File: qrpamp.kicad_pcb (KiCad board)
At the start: 2 copper layers, 152.4 x 88.9 mm, 113 parts, among them K1 BAND3_IN, K2 BAND2_IN, K3 BAND1_IN, K4 BAND3_OUT, K5 BAND2_OUT, K6 BAND1_OUT, K7 ANT_RLY, P1 PWR, P2 PWR_SW, P3 SWD, P4 ANT, P5 RADIO, P6 PTT_IN, P7 TP, P8 NAV_BUTTON, Q1 MMBT6427, Q10 MMBF170, Q11 MMBF170, Q2 MMBF170, Q3 IRF510, Q4 IRF510, Q6 MMBF170, Q9 MMBF170, SW1 SW_PUSH, T1 8:8, T2 8:8, T3 2:3, T4 12:1, T5 1:12, U1 LM7805, U2 LM3940, U3 LCD-2x16, U4 STM32F401xB/C-LQFP

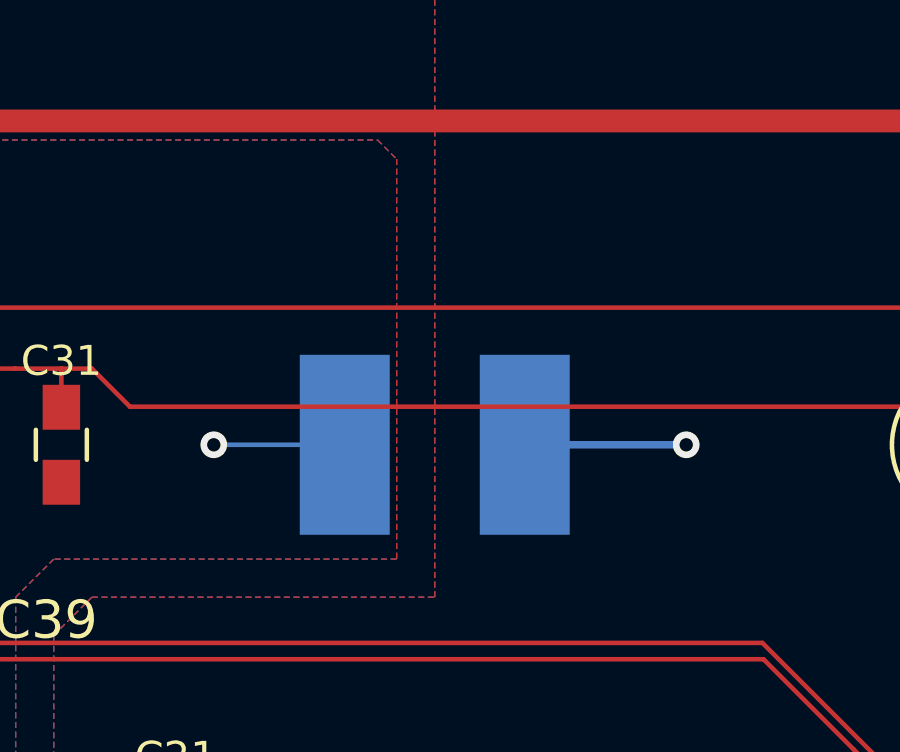
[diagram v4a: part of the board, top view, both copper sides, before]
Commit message: Closes #4: extend chassis pads
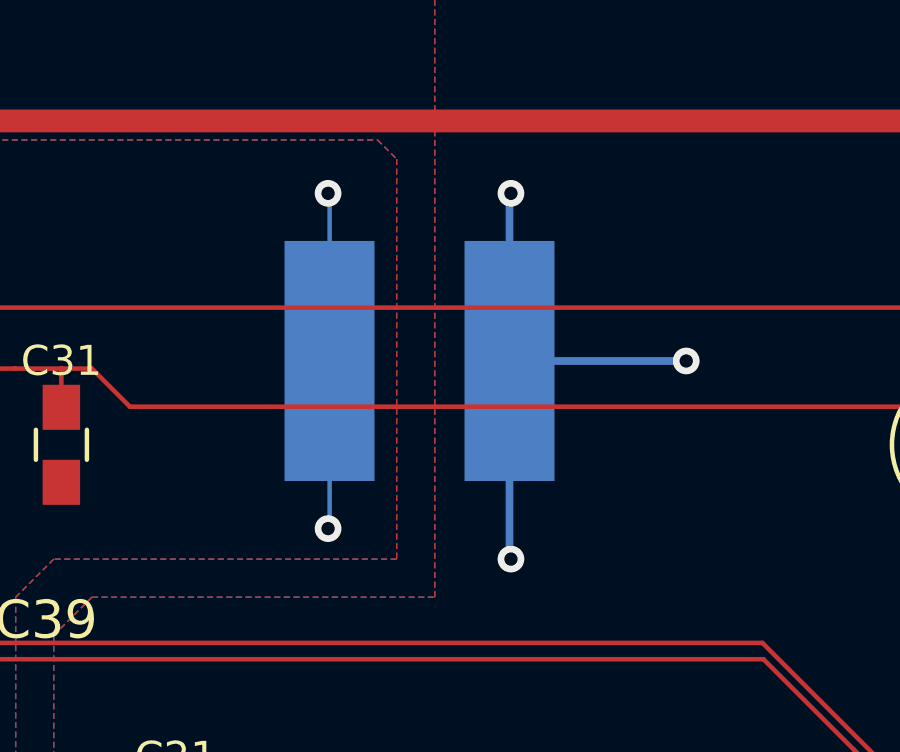
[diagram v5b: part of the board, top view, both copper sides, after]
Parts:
- moved L9 2.84 mm to (132.8, 55.6)
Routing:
- net GND: track 61.4 -> 74.1 mm, vias 13 -> 15
- net DGND: track 27.2 -> 34.0 mm, vias 7 -> 8
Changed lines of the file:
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@@
     (thickness 1.6)
     (drawings 26)
-    (tracks 693)
+    (tracks 703)
     (zones 0)
     (modules 113)
@@
     (mod_text_size 1.5 1.5)
     (mod_text_width 0.15)
-    (pad_size 0.8001 1.80086)
+    (pad_size 2.99974 8)
     (pad_drill 0)
     (pad_to_mask_clearance 0.2)
@@
   )
   (module nu9j-footprints:WE-SUCKW (layer B.Cu)
-    (at 133.35 58.42 180)
+    (at 132.842 55.626 180)
     (fp_text reference L9 (at 0 5.00126 180) (layer B.SilkS)
       (effects (font (thickness 0.3048)) (justify mirror))
@@
     (fp_line (start 5.99948 -2.49936) (end 5.99948 2.49936) (layer B.SilkS) (width 0.381))
     (fp_line (start 5.99948 2.49936) (end -5.99948 2.49936) (layer B.SilkS) (width 0.381))
-    (pad 1 smd rect (at -2.99974 0 180) (size 2.99974 5.99948) (layers B.Cu B.Paste B.Mask)
+    (pad 1 smd rect (at -2.99974 0 180) (size 2.99974 8) (layers B.Cu B.Paste B.Mask)
       (net 3 GND))
-    (pad 2 smd rect (at 2.99974 0 180) (size 2.99974 5.99948) (layers B.Cu B.Paste B.Mask)
+    (pad 2 smd rect (at 2.99974 0 180) (size 2.99974 8) (layers B.Cu B.Paste B.Mask)
       (net 85 DGND))
   )
@@
   (segment (start 206.756 102.87) (end 213.36 102.87) (width 0.2794) (layer F.Cu) (net 2))
   (segment (start 209.53 92.71) (end 211.582 92.71) (width 0.2794) (layer F.Cu) (net 2))
+  (segment (start 135.84174 55.626) (end 135.84174 50.08626) (width 0.254) (layer B.Cu) (net 3))
+  (via (at 135.89 50.038) (size 0.889) (layers F.Cu B.Cu) (net 3))
+  (segment (start 135.84174 50.08626) (end 135.89 50.038) (width 0.254) (layer B.Cu) (net 3))
+  (segment (start 135.84174 55.626) (end 135.84174 62.18174) (width 0.254) (layer B.Cu) (net 3))
+  (via (at 135.89 62.23) (size 0.889) (layers F.Cu B.Cu) (net 3))
+  (segment (start 135.84174 62.18174) (end 135.89 62.23) (width 0.254) (layer B.Cu) (net 3))
+  (segment (start 135.84174 55.626) (end 141.732 55.626) (width 0.254) (layer B.Cu) (net 3))
+  (via (at 141.732 55.626) (size 0.889) (layers F.Cu B.Cu) (net 3))
   (segment (start 215.41486 109.662) (end 215.41486 111.02086) (width 0.254) (layer F.Cu) (net 3))
   (via (at 216.662 112.268) (size 0.889) (layers F.Cu B.Cu) (net 3))
@@
   (via (at 185.42 124.714) (size 0.889) (layers F.Cu B.Cu) (net 3))
   (segment (start 185.42 121.38) (end 185.42 124.714) (width 0.254) (layer F.Cu) (net 3))
-  (via (at 141.732 58.42) (size 0.889) (layers F.Cu B.Cu) (net 3))
-  (segment (start 136.34974 58.42) (end 141.732 58.42) (width 0.254) (layer B.Cu) (net 3))
   (segment (start 197.58 78.74) (end 197.58 82.55) (width 0.254) (layer F.Cu) (net 4))
   (segment (start 201.95 78.74) (end 197.58 78.74) (width 0.254) (layer F.Cu) (net 4))
@@
   (segment (start 100.838 70.358) (end 103.632 70.358) (width 0.1524) (layer F.Cu) (net 79))
   (segment (start 100.484 70.004) (end 100.838 70.358) (width 0.1524) (layer F.Cu) (net 79))
+  (segment (start 129.84226 55.626) (end 129.84226 61.16574) (width 0.1524) (layer B.Cu) (net 85))
+  (via (at 129.794 61.214) (size 0.889) (layers F.Cu B.Cu) (net 85))
+  (segment (start 129.84226 61.16574) (end 129.794 61.214) (width 0.1524) (layer B.Cu) (net 85))
+  (segment (start 129.84226 55.626) (end 129.84226 50.08626) (width 0.1524) (layer B.Cu) (net 85))
+  (via (at 129.794 50.038) (size 0.889) (layers F.Cu B.Cu) (net 85))
+  (segment (start 129.84226 50.08626) (end 129.794 50.038) (width 0.1524) (layer B.Cu) (net 85))
   (segment (start 109.22 58.4) (end 109.22 60.198) (width 0.1524) (layer F.Cu) (net 85))
   (via (at 109.982 60.96) (size 0.889) (layers F.Cu B.Cu) (net 85))
@@
   (via (at 92.075 55.88) (size 0.889) (layers F.Cu B.Cu) (net 85))
   (segment (start 92.476 53.594) (end 92.476 55.479) (width 0.1524) (layer F.Cu) (net 85))
-  (via (at 125.984 58.42) (size 0.889) (layers F.Cu B.Cu) (net 85))
-  (segment (start 130.35026 58.42) (end 125.984 58.42) (width 0.1524) (layer B.Cu) (net 85))
   (segment (start 130.81 116.84) (end 130.81 111.76) (width 0.254) (layer F.Cu) (net 86))
   (segment (start 128.27 109.22) (end 128.27 101.6) (width 0.254) (layer F.Cu) (net 86))

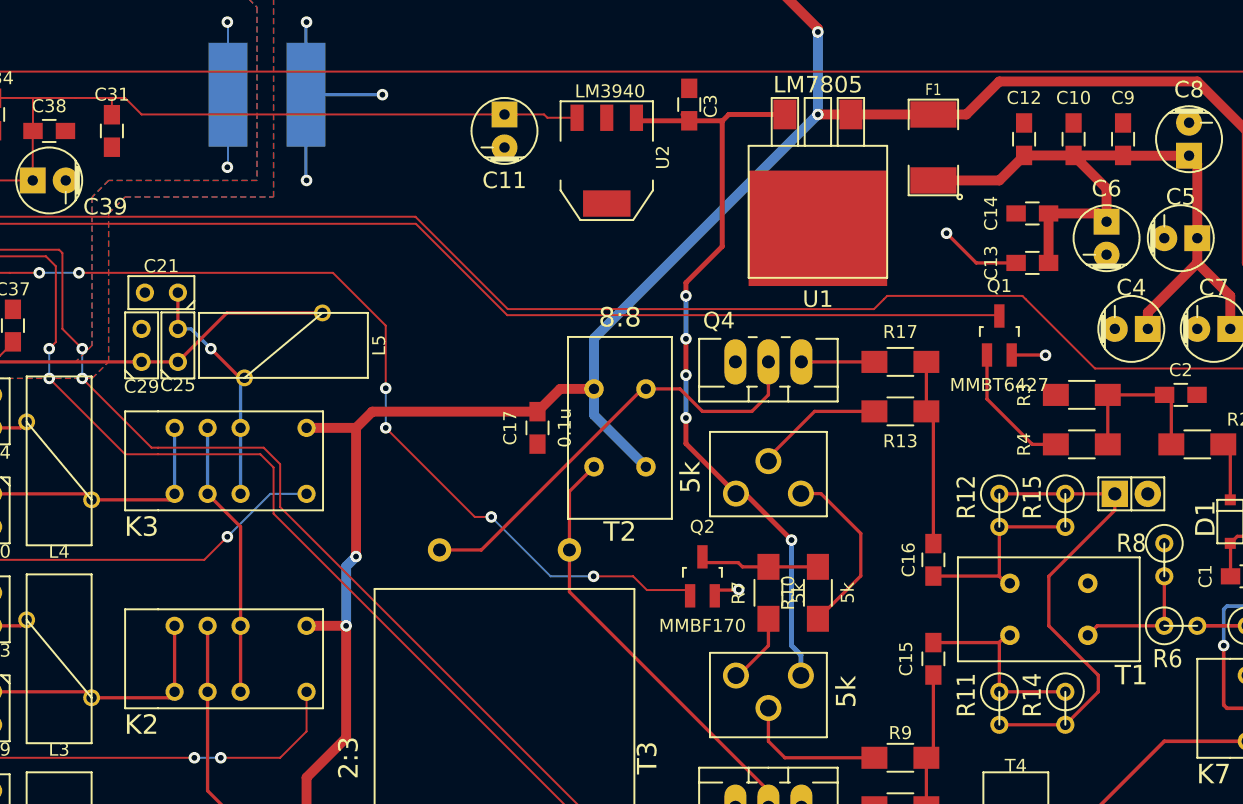
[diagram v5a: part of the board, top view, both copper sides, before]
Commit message: Fixes #9: gate bias broken
Replaces Q2 with LTV-356T opto-coupler between 5V and bias rail
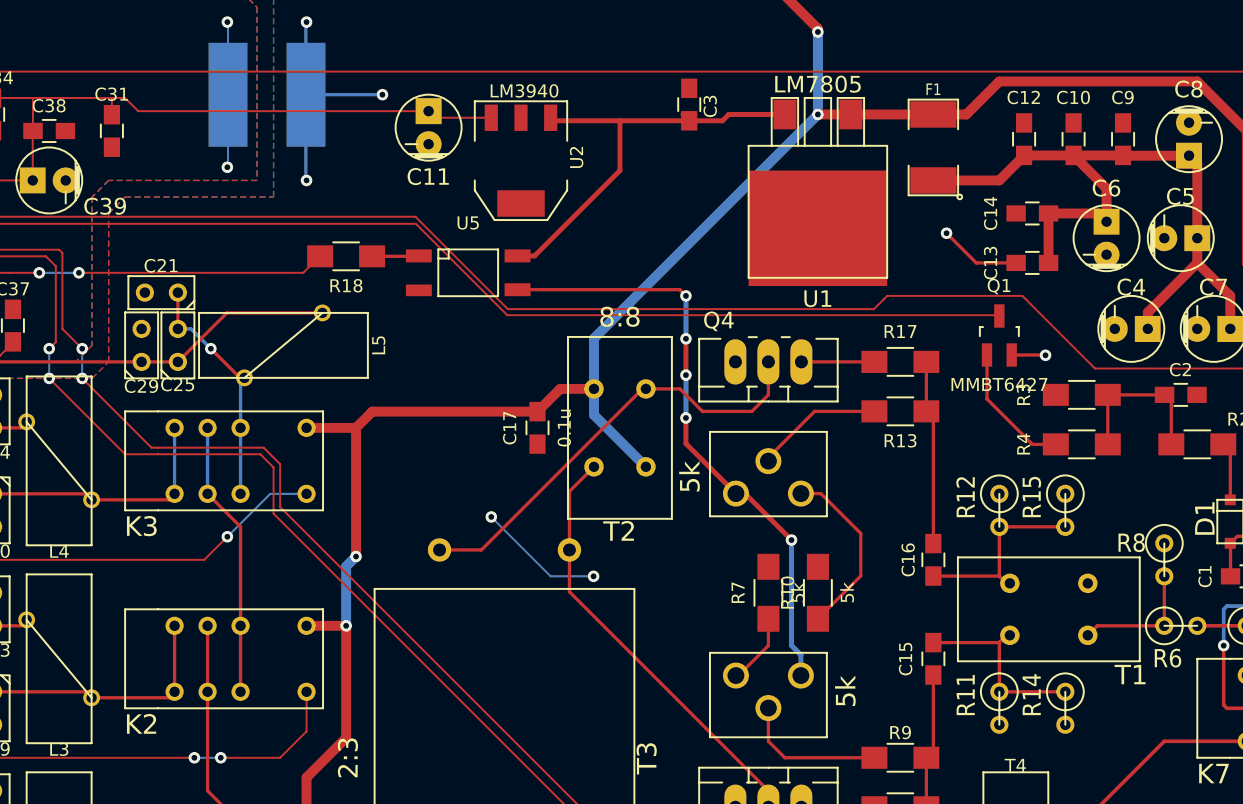
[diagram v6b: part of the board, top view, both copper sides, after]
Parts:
- removed JP1: AMP_BAL, Pin_Headers:Pin_Header_Straight_1x02
- removed Q2: MMBF170, nu9j-footprints:SOT-23-DGS_HandSoldering
- added R18: 150, Resistors_SMD:R_1206_HandSoldering, F.Cu at (138.9, 68.1)
- added U5: LTV-356T, Opto-Devices:Optocoupler_SMD_HandSoldering_KPC357_LTV35x_PC357_SingleChannel, F.Cu at (148.3, 69.3)
- moved U2 6.60 mm to (152.4, 60.7)
- moved C11 5.85 mm to (145.3, 58.2)
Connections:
- R10 pad 2: Net-(Q2-PadD) -> GND
- R11 pad 2: Net-(JP1-Pad1) -> GND
- R12 pad 1: Net-(JP1-Pad1) -> GND
- R14 pad 2: Net-(JP1-Pad1) -> GND
- R15 pad 1: Net-(JP1-Pad1) -> GND
- R7 pad 2: Net-(Q2-PadD) -> GND
- RV1 pad 1: +5V -> Net-(RV1-Pad1)
- RV2 pad 1: +5V -> Net-(RV1-Pad1)
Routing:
- net Net-(RV1-Pad1): track 0.00 -> 46.5 mm, vias 0 -> 5
- net /Amplifier/amp_on: track 85.5 -> 42.8 mm, vias 6 -> 2
- net Net-(JP1-Pad1): track 36.5 -> 0.00 mm
- net +5V: track 60.4 -> 33.5 mm, vias 5 -> 0
- net (no net): track 0.02 -> 9.79 mm, vias 0 -> 2
- net Net-(Q2-PadD): track 9.49 -> 0.00 mm
- net +3.3V: track 146.8 -> 140.2 mm
- net Net-(R18-Pad1): track 0.00 -> 3.61 mm
- net GND: track 74.1 -> 72.7 mm, vias 15 -> 14

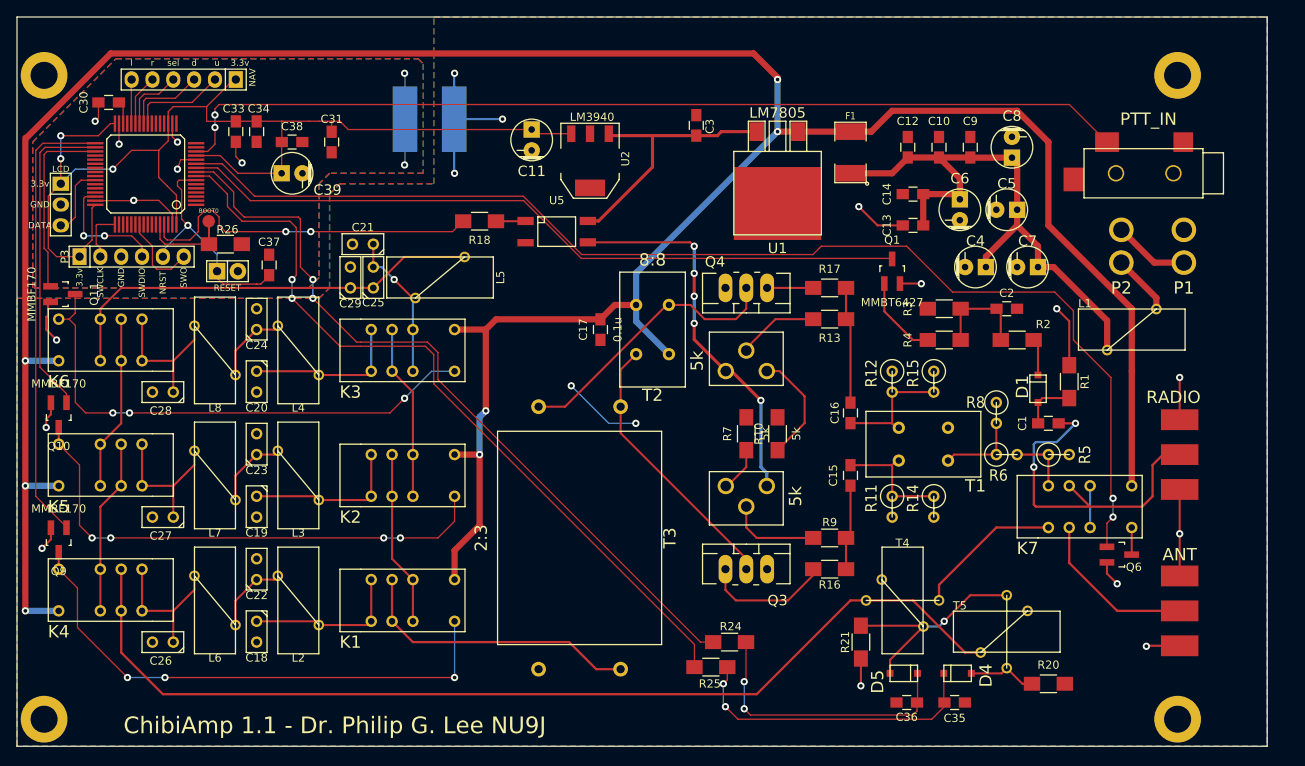
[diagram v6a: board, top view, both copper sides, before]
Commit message: Fixes #8: transistor placement
Also, this is a major board layout change

- Added more 12V filtering caps
- Placed fuse in front of filtering caps
- Changed IRF510 footprints to horizontal lower side w/ mounting hole
- Expanded layout to fill new board size
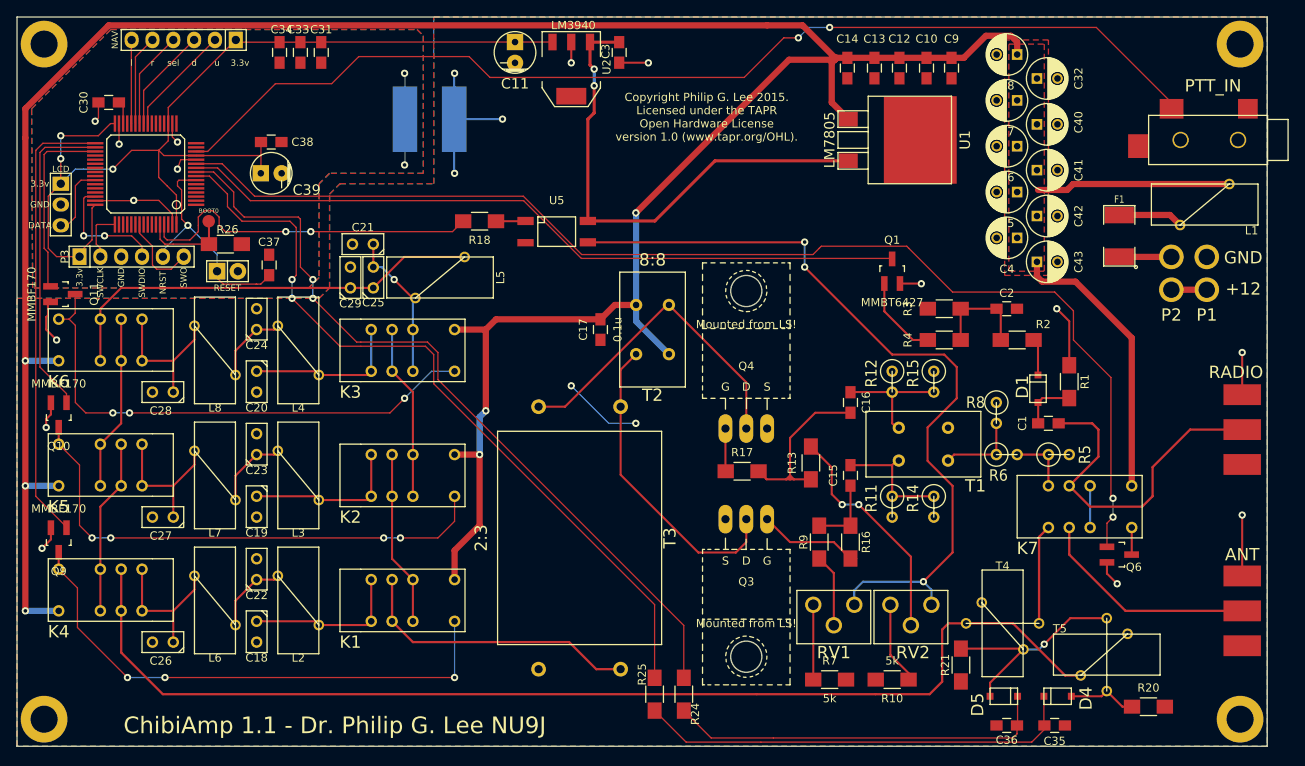
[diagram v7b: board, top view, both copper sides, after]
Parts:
- added C32: 10u, Capacitors_ThroughHole:C_Radial_D5_L11_P2.5, F.Cu at (206.9, 50.7)
- added C40: 10u, Capacitors_ThroughHole:C_Radial_D5_L11_P2.5, F.Cu at (206.9, 56.3)
- added C41: 10u, Capacitors_ThroughHole:C_Radial_D5_L11_P2.5, F.Cu at (206.9, 61.8)
- added C42: 10u, Capacitors_ThroughHole:C_Radial_D5_L11_P2.5, F.Cu at (206.9, 67.4)
- added C43: 10u, Capacitors_ThroughHole:C_Radial_D5_L11_P2.5, F.Cu at (206.9, 73.0)
- C4, C5, C6, C7, C8: footprint Capacitors_ThroughHole:Capacitor5x11RM2.5 -> Capacitors_ThroughHole:C_Radial_D5_L11_P2.5
- F1: value PTS181224V150 -> PTS18128V200
- Q3, Q4: footprint Transistors_TO-220:TO-220_FET-GDS_Vertical_LargePads -> Transistors_TO-220:TO-220_FET-GDS_Horizontal_MountedFromLS_LargePads
- moved RV2 36.9 mm to (191.5, 116.1), turned to 90 degrees
- moved F1 34.3 mm to (216.9, 69.8)
- moved R10 33.1 mm to (189.2, 124.0), turned to 180 degrees
- moved R7 31.6 mm to (181.6, 124.0), turned to 0 degrees
- moved R17 24.8 mm to (170.9, 98.6)
- moved C7 20.4 mm to (204.5, 53.3), turned to 180 degrees
- moved C13 19.7 mm to (187.1, 49.4), turned to 270 degrees
- moved RV1 18.0 mm to (182.1, 116.1)
- moved R13 17.7 mm to (179.3, 97.5), turned to 90 degrees
- moved L1 17.6 mm to (227.3, 66.0), turned to 90 degrees
- moved C14 17.3 mm to (183.8, 49.4), turned to 270 degrees
- moved Q4 17.1 mm to (171.4, 93.3), turned to 0 degrees
- moved C3 12.9 mm to (156.0, 47.5), turned to 270 degrees
- moved R20 12.5 mm to (220.5, 127.3)
- moved R21 12.5 mm to (197.6, 122.2)
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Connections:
- C10 pad 1: Net-(C10-Pad1) -> +12V
- C12 pad 1: Net-(C10-Pad1) -> +12V
- C13 pad 1: Net-(C10-Pad1) -> +12V
- C14 pad 1: Net-(C10-Pad1) -> +12V
- C4 pad 1: Net-(C10-Pad1) -> +12V
- C5 pad 1: Net-(C10-Pad1) -> +12V
- C6 pad 1: Net-(C10-Pad1) -> +12V
- C7 pad 1: Net-(C10-Pad1) -> +12V
- C8 pad 1: Net-(C10-Pad1) -> +12V
- C9 pad 1: Net-(C10-Pad1) -> +12V
- F1 pad 1: Net-(C10-Pad1) -> Net-(F1-Pad1)
- F1 pad 2: +12V -> Net-(F1-Pad2)
- L1 pad 1: Net-(L1-Pad1) -> Net-(F1-Pad2)
- L1 pad 2: Net-(C10-Pad1) -> +12V
- P2 pad 2: Net-(L1-Pad1) -> Net-(F1-Pad1)
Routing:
- net Net-(C10-Pad1): track 71.3 -> 0.00 mm
- net Net-(RV1-Pad1): track 46.5 -> 97.3 mm, vias 5 -> 3
- net +12V: track 349.7 -> 379.2 mm, vias 7 -> 6
- net +5V: track 33.5 -> 60.7 mm, vias 0 -> 2
- net Net-(R13-Pad2): track 10.6 -> 28.0 mm, vias 0 -> 2
- net /Microcontroller/mcu_swr_ref: track 37.2 -> 53.8 mm, vias 2 -> 0
- net /Band Filters/bandfilter_out: track 124.4 -> 139.2 mm
- net /Microcontroller/mcu_ptt: track 118.9 -> 133.6 mm
- net /Microcontroller/mcu_swr_fwd: track 34.7 -> 46.8 mm, vias 2 -> 0
- net GND: track 72.7 -> 61.5 mm, vias 14 -> 13
- net +3.3V: track 140.2 -> 130.2 mm
- net Net-(L1-Pad1): track 8.82 -> 0.00 mm
- net Net-(F1-Pad2): track 0.00 -> 7.92 mm
- net /Amplifier/vb2: track 14.2 -> 21.8 mm
- net Net-(K7-Pad9): track 20.2 -> 27.2 mm
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- added copper zone on F.Cu, net +12V

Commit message: Silkscreen cleanup
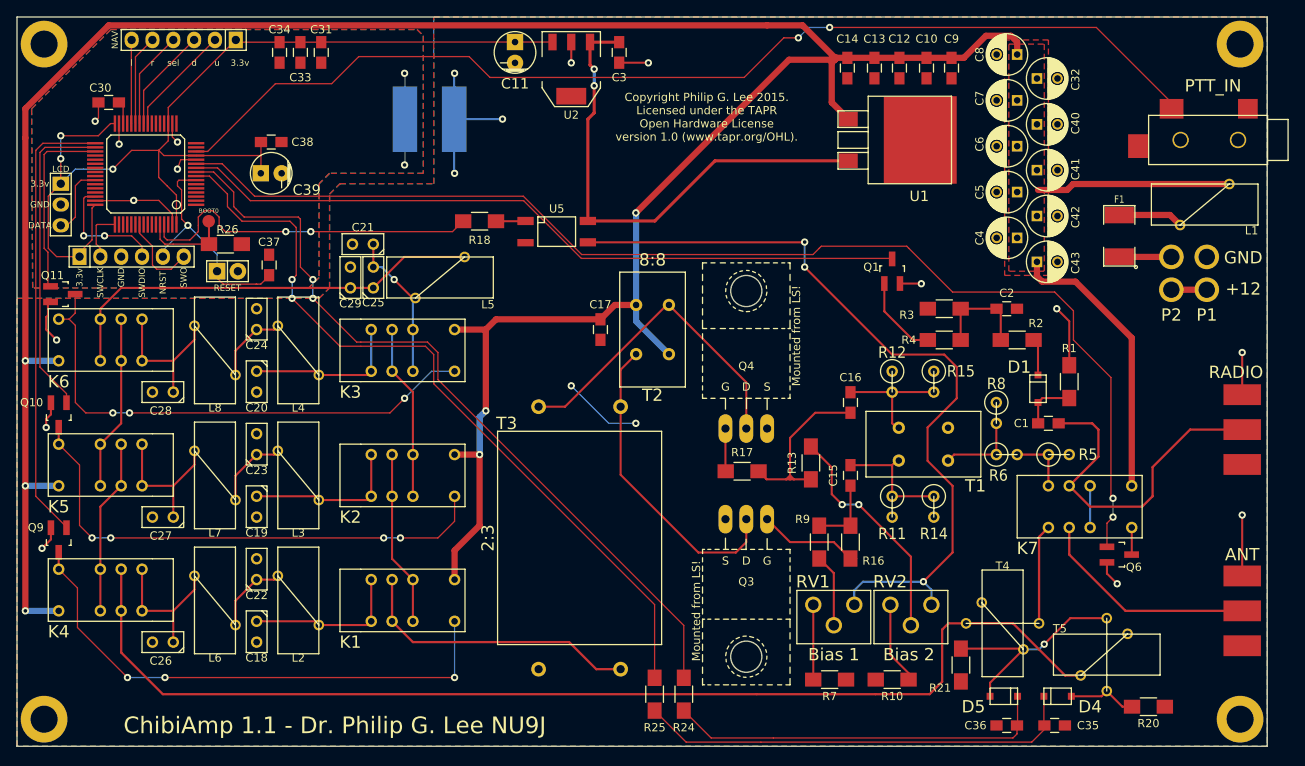
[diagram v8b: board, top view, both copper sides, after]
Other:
- board text added: "Bias 1"
- board text added: "Bias 2"
